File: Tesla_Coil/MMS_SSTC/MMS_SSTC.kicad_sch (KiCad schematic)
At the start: 13 parts, among them J2 Screw_Terminal_01x02, Q1 IRFP460APBF

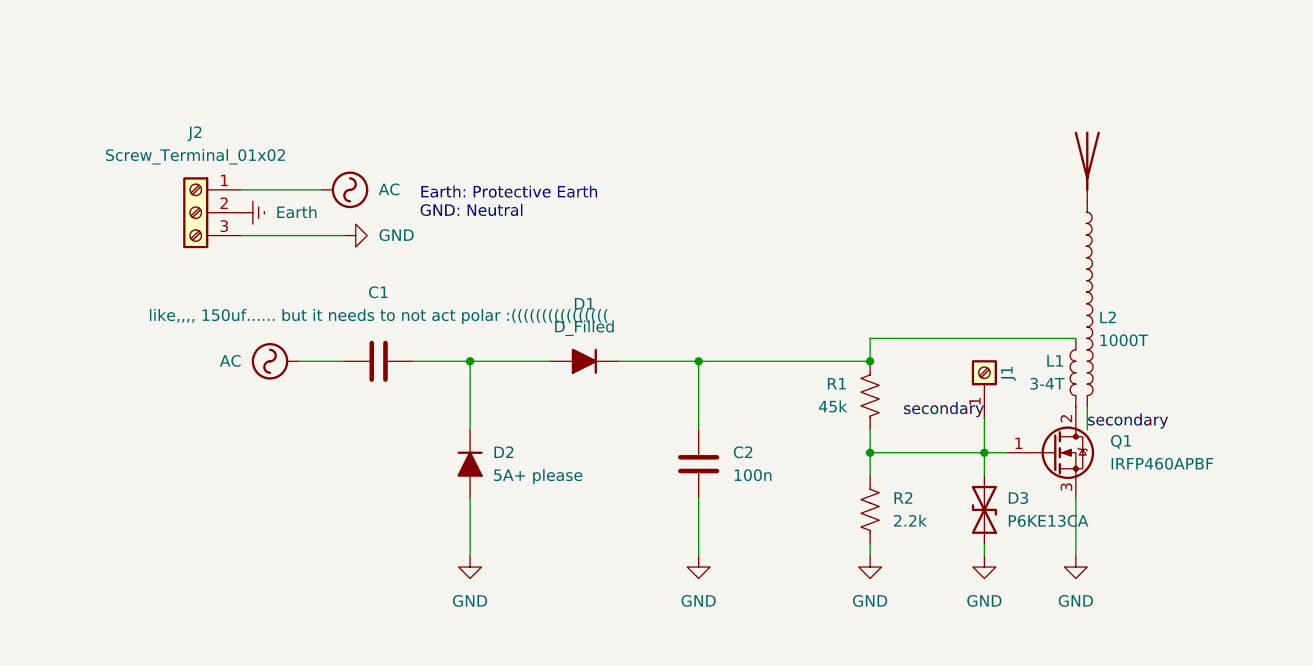
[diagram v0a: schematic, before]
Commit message: update gitignore
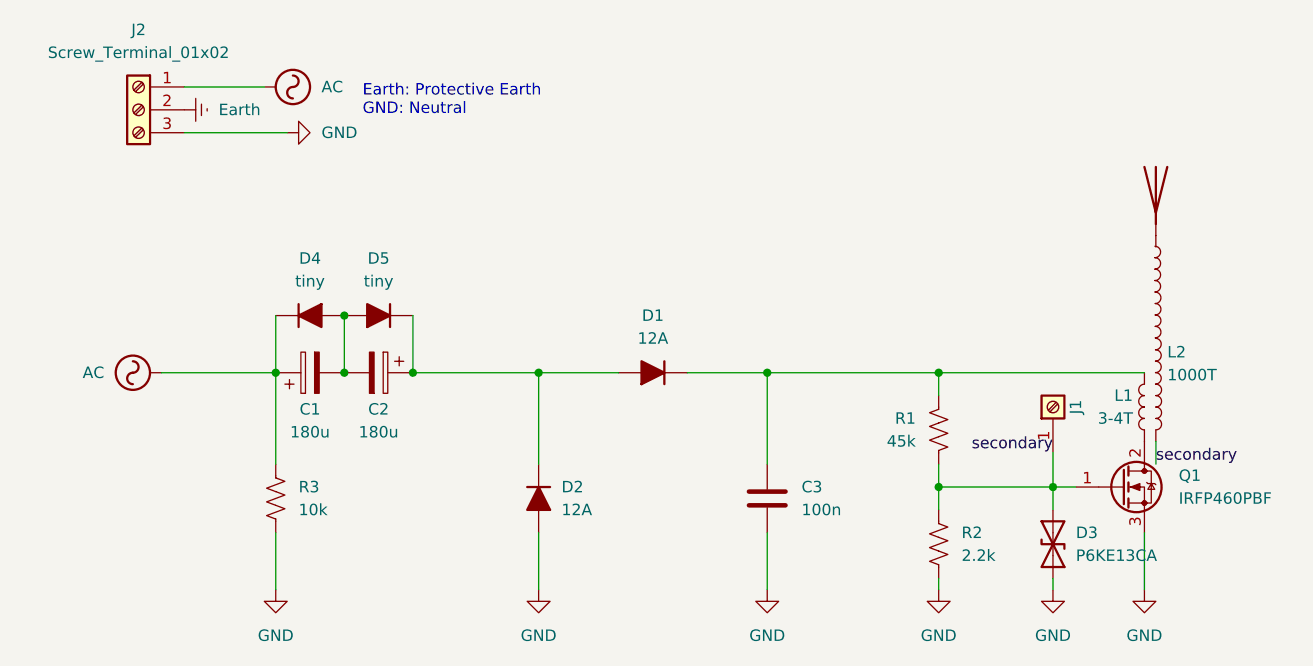
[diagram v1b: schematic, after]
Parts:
- removed C1: like,,,, 150uf...... but it needs to not act pola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, symbol Device:C
- added C1, C2: 180u, symbol Device:C_Polarized
- added D4, D5: tiny, Diode_THT:D_DO-201AD_P15.24mm_Horizontal, symbol Device:D_Filled
- added R3: 10k, symbol Device:R_US
- D1: value D_Filled -> 12A
- D2: value 5A+ please -> 12A
- Q1: value IRFP460APBF -> IRFP460PBF
- renumbered C2 to C3
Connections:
- net AC: now also C1.1, D4.1 (K), R3.1
- net GND: now also R3.2
- net at D1.2 (A), D2.1 (K): now also C2.1, D5.1 (K)
- new net: C1.2, C2.2, D4.2 (A), D5.2 (A)
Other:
- moved on the sheet: C3, D1, D2, D3, J1, J2, L1, L2, Q1, R1, R2

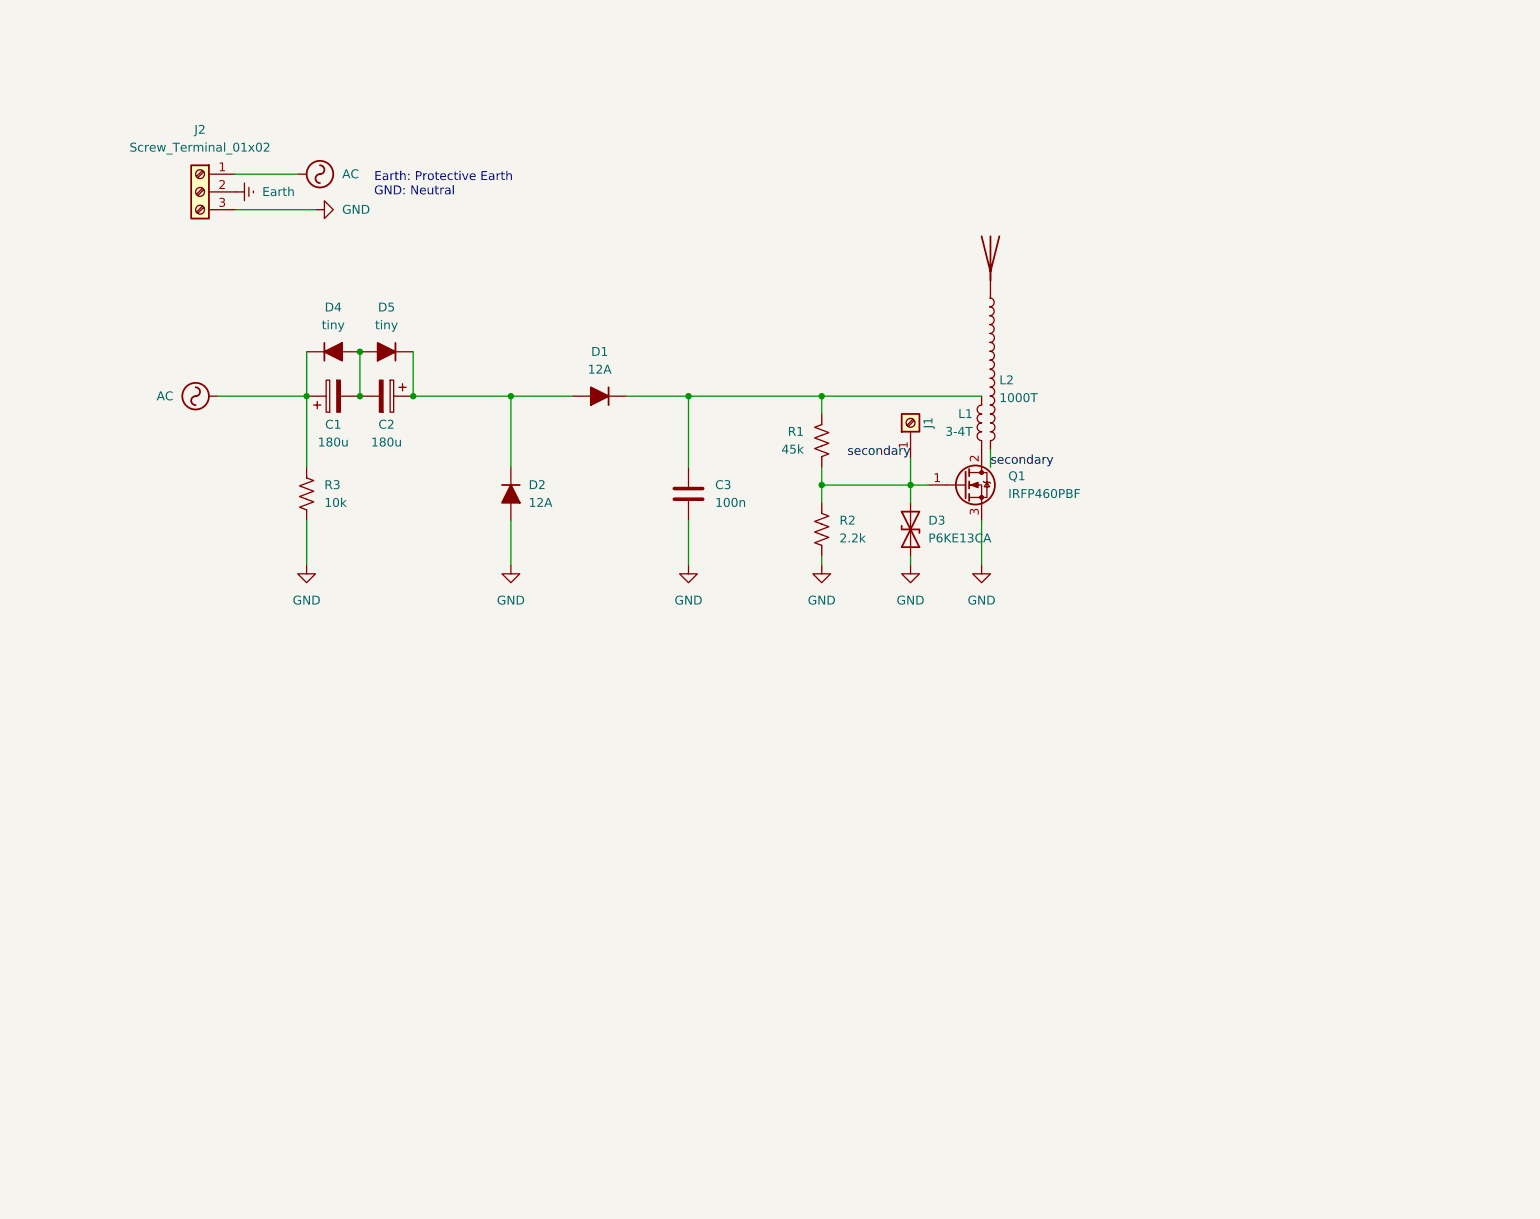
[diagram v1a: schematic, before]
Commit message: Progress save for modification on schematic. Nowhere near done
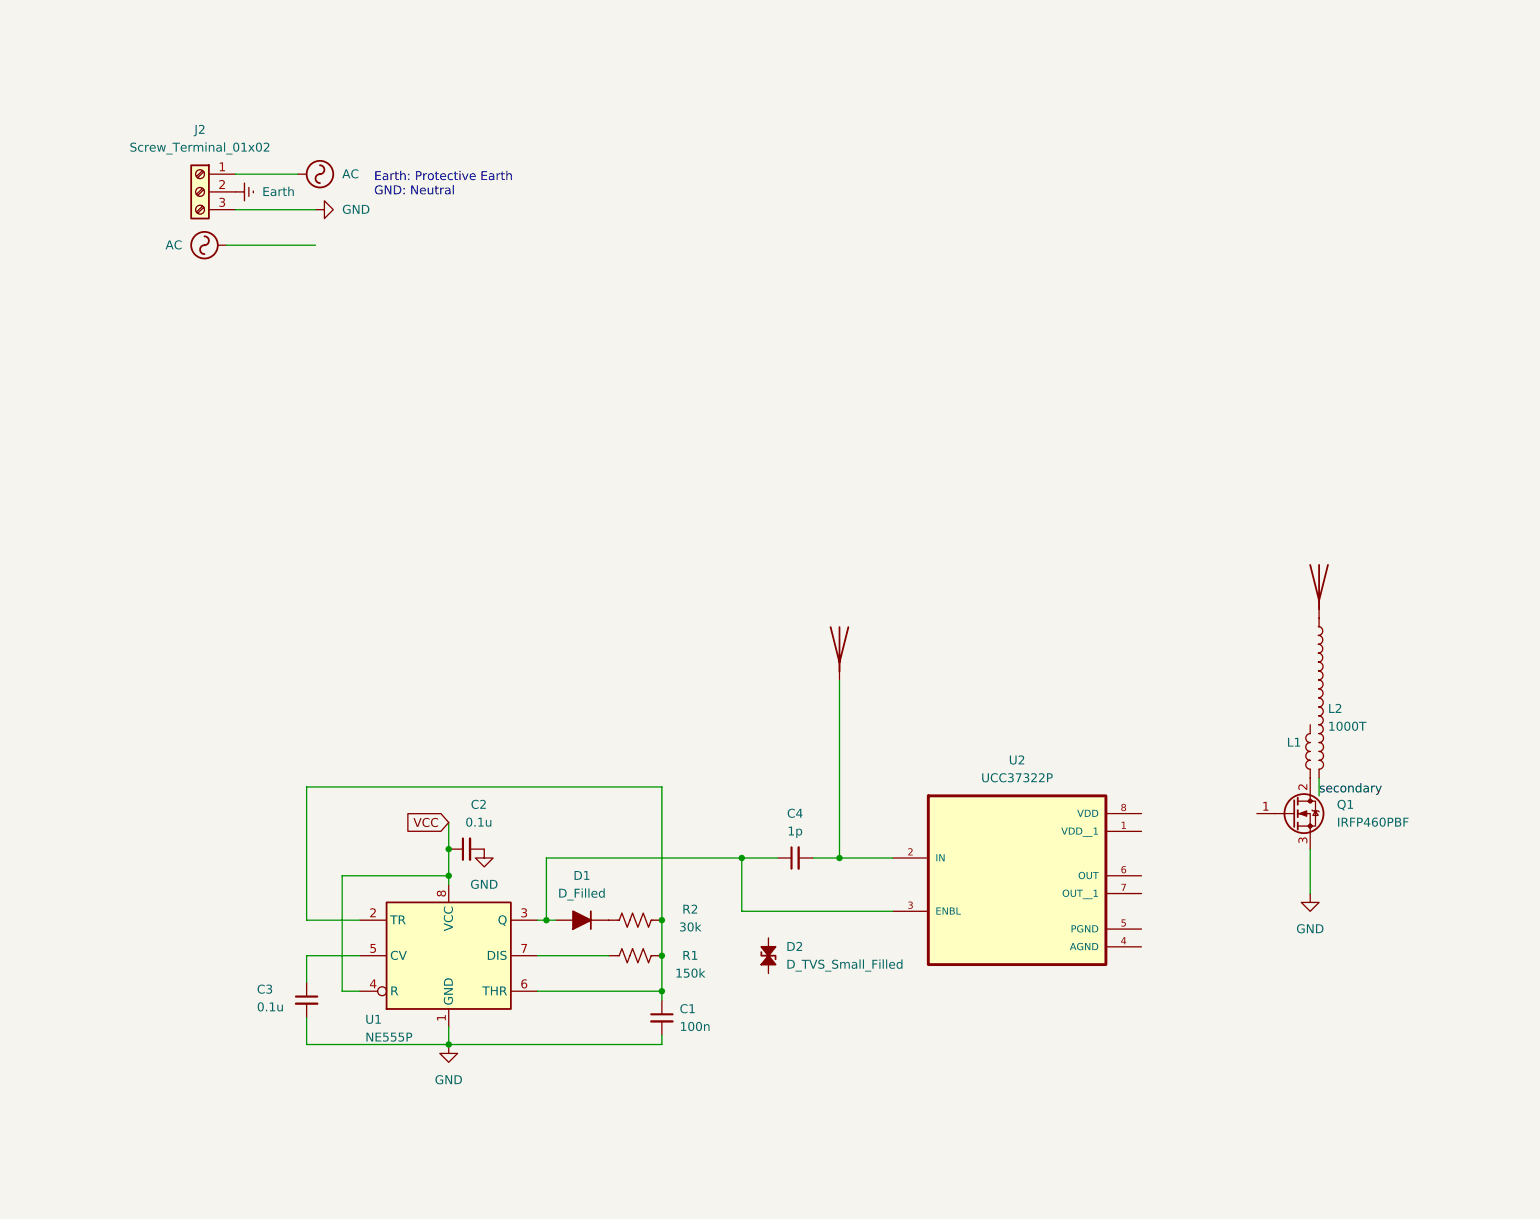
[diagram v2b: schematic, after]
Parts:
- removed C1, C2: 180u, symbol Device:C_Polarized
- removed C3: 100n, locals:CAPRR1500W80L1800T500H1050, symbol Device:C
- removed D2: 12A, Diode_THT:D_DO-201AD_P15.24mm_Horizontal, symbol Device:D_Filled
- removed D3: P6KE13CA, Diode_THT:D_DO-201AE_P15.24mm_Horizontal, symbol Diode:1N62xxCA
- removed D4, D5: tiny, Diode_THT:D_DO-201AD_P15.24mm_Horizontal, symbol Device:D_Filled
- removed J1: ~, locals:CONN_360410_MZC, symbol Connector:Screw_Terminal_01x01
- removed R3: 10k, symbol Device:R_US
- added AE2: Antenna, symbol Device:Antenna
- added C1: 100n, symbol Device:C_Small
- added C2, C3: 0.1u, symbol Device:C_Small
- added C4: 1p, symbol Device:C_Small
- added D2: D_TVS_Small_Filled, symbol Device:D_TVS_Small_Filled
- added U1: NE555P, Package_DIP:DIP-8_W7.62mm, symbol Timer:NE555P
- added U2: UCC37322P, UCC37322P:DIP794W45P254L959H508Q8, symbol locals:UCC37322P
- D1: value 12A -> D_Filled; footprint Diode_THT:D_DO-201AD_P15.24mm_Horizontal -> (none); DKPN SBR12A45SD1-TDICT-ND -> (none)
- R1: value 45k -> 150k; DKPN 2019-CF1/2CT52R301JCT-ND -> (none)
- R2: value 2.2k -> 30k; DKPN A105894CT-ND -> (none)
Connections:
- net GND: now also C1.2, C2.2, C3.2, U1.1 (GND); no longer R2.2
- net secondary: no longer Q1.1 (G), R1.2, R2.1
- net at D1.2 (A): now also C4.1, U1.3 (Q), U2.3 (ENBL)
- new net: C3.1, U1.5 (CV)
- new net: C1.1, R1.2, R2.2, U1.2 (TR), U1.6 (THR)
- new net: D1.1 (K), R2.1
- new net: AE2.1 (A), C4.2, U2.2 (IN)
- new net: R1.1, U1.7 (DIS)
- new net VCC: C2.1, U1.4 (R), U1.8 (VCC)
- now unconnected: L1.1
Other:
- moved on the sheet: L1, L2, Q1

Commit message: Updated schematic for prototype PCB - needs DKPNs and final review still
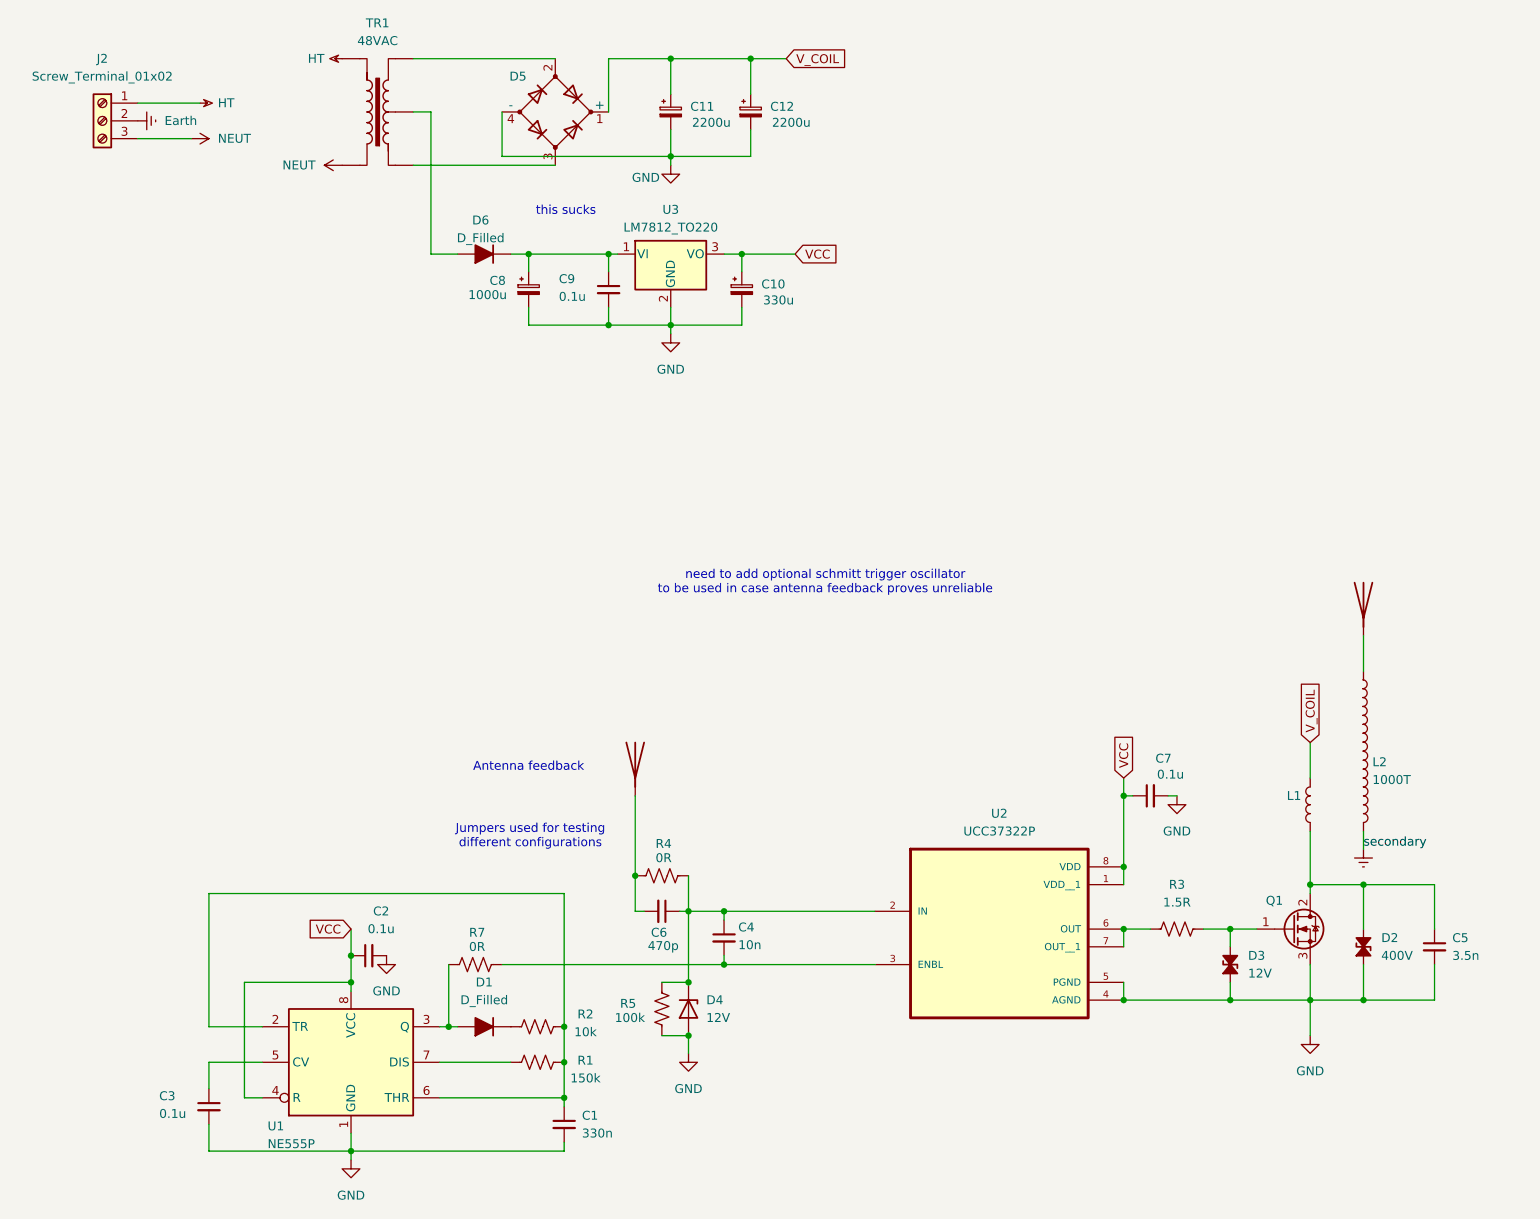
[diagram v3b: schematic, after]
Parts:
- added C10: 330u, symbol Device:C_Polarized_Small
- added C11, C12: 2200u, symbol Device:C_Polarized_Small
- added C5: 3.5n, symbol Device:C_Small
- added C6: 470p, symbol Device:C_Small
- added C7, C9: 0.1u, symbol Device:C_Small
- added C8: 1000u, symbol Device:C_Polarized_Small
- added D3: 12V, symbol Device:D_TVS_Small_Filled
- added D4: 12V, symbol Device:D_Zener
- added D5: D_Bridge_+AA-, symbol Device:D_Bridge_+AA-
- added D6: D_Filled, symbol Device:D_Filled
- added R3: 1.5R, symbol Device:R_US
- added R4, R7: 0R, symbol Device:R_US
- added R5: 100k, symbol Device:R_US
- added TR1: 48VAC, symbol Transformer:TRANSF4
- added U3: LM7812_TO220, Package_TO_SOT_THT:TO-220-3_Vertical, symbol Regulator_Linear:LM7812_TO220
- C1: value 100n -> 330n
- C4: value 1p -> 10n
- D2: value D_TVS_Small_Filled -> 400V
- Q1: value IRFP460PBF -> IRFP460APBF; DKPN IRFP460PBF-ND -> IRFP460APBF-ND
- R2: value 30k -> 10k
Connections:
- net secondary is gone; now on net Earth: L2.2
- net GND: now also D2.1 (A1), U2.4 (AGND), U2.5 (PGND), C10.2, C11.2, C12.2, C5.2, C7.2, C8.2, C9.2, D3.1 (A1), D4.2 (A), D5.4 (-), R5.1, U3.2 (GND); no longer J2.3 (Pin_3)
- net VCC: now also U2.1 (VDD__1), U2.8 (VDD), C10.1, C7.1, U3.3 (VO)
- net V_COIL: now reaches L1.1
- net V_COIL: now also C11.1, C12.1, D5.1 (+)
- net at L1.2, Q1.2 (D): now also D2.2 (A2), C5.1
- net at D1.2 (A), U1.3 (Q): now also R7.2; no longer C4.1, U2.3 (ENBL)
- net at U2.6 (OUT): now also U2.7 (OUT__1), R3.1
- net at Q1.1 (G): now also D3.2 (A2), R3.2
- net AC renamed HT
- net HT: now also TR1.4
- new net: C4.1, C6.1, D4.1 (K), R4.1, R5.2, U2.2 (IN)
- new net: C4.2, R7.1, U2.3 (ENBL)
- new net: D5.3, TR1.1
- new net: D6.2 (A), TR1.2
- new net: D5.2, TR1.3
- new net: AE2.1 (A), C6.2, R4.2
- new net: C8.1, C9.1, D6.1 (K), U3.1 (VI)
- new net NEUT: J2.3 (Pin_3), TR1.5
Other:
- note added: "Antenna feedback"
- note added: "Jumpers used for testing different configurations"
- note added: "need to add optional schmitt trigger oscillator to be used in case antenna feedback proves unreliable"
- note added: "this sucks"
- note removed: "Earth: Protective Earth GND: Neutral"
- moved on the sheet: C1, C2, C3, D1, D2, J2, L1, L2, Q1, R1, R2, U1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
